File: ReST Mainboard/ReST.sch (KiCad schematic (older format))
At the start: 17 parts

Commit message: Added ReST connector to the Mainboard
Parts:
- added P?: CONN_02X04, symbol CONN_02X04
- added P? (x7): CONN_02X08, symbol CONN_02X08
- added P? (x4): CONN_02X10, symbol CONN_02X10
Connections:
- net labels added: +12V, +3.3V, +5V, E0-DIR, E0-EN, E0-MAX, E0-MIN, E0-STEP, E1-DIR, E1-EN, E1-MAX, E1-MIN, E1-STEP, E2-DIR, E2-EN, E2-MAX, E2-MIN, E2-STEP, E3-DIR, E3-EN, E3-MAX, E3-MIN, E3-STEP, PWM-BED, PWM-HEAT1, PWM-HEAT2, PWM-HEAT3, PWM-HEAT4, T0, T1, T2, T3, T4, X-DIR, X-EN, X-MAX, X-MIN, X-STEP, Y-DIR, Y-EN, Y-MAX, Y-MIN, Y-STEP, Z-DIR, Z-EN, Z-MAX, Z-MIN, Z-STEP
- wire segments 84 -> 302
- no-connect marks 0 -> 7
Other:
- note added: "Heatbed Connector"
- note added: "Heater Output 1"
- note added: "Heater Output 2"
- note added: "Heater Output 3"
- note added: "Heater Output 4"
- note added: "Stepper E0"
- note added: "Stepper E1"
- note added: "Stepper E2"
- note added: "Stepper E3"
- note added: "Stepper X"
- note added: "Stepper Y"
- note added: "Stepper Z"

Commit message: Added Pololu to the Mainboard
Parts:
- removed P? (x7): CONN_02X08, symbol CONN_02X08
- added C?: 10nF, symbol C_Small
- added C?: 100uF, symbol CP1_Small
- added P?: CONN_02X03, symbol CONN_02X03
- added P?: CONN_02X04, symbol CONN_02X04
- added P?: SCREW_01X04, symbol CONN_01X04
- added P?: CONN_01X03, symbol CONN_01X03
- added P? (x2): SCREW_01X03, symbol CONN_01X03
- added R?: 100K, symbol R_Small
- added U?: POLOLU_A4988, symbol POLOLU_A4988
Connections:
- net labels added: ENDSTOP_VCC
- net labels removed: E0-DIR, E0-EN, E0-MAX, E0-MIN, E0-STEP, E1-DIR, E1-EN, E1-MAX, E1-MIN, E1-STEP, E2-DIR, E2-EN, E2-MAX, E2-MIN, E2-STEP, E3-DIR, E3-EN, E3-MAX, E3-MIN, E3-STEP, X-DIR, X-EN, X-MAX, X-MIN, X-STEP, Y-DIR, Y-EN, Y-MAX, Y-MIN, Y-STEP, Z-DIR, Z-EN, Z-MAX, Z-MIN, Z-STEP
- wire segments 302 -> 227
- no-connect marks 7 -> 0
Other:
- note removed: "Stepper E0"
- note removed: "Stepper E1"
- note removed: "Stepper E2"
- note removed: "Stepper E3"
- note removed: "Stepper X"
- note removed: "Stepper Y"
- note removed: "Stepper Z"

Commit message: Changes to the mainboard
removed the pololu connector, added it onboard. added 5V regulator. need to add 3.3V Regulator and more pinout (Bluetooth, SWD, Boot0/Boot1 and more)
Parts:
- removed C? (x11): 100nF, symbol C_Small
- removed C?: 4.7uF, symbol C_Small
- removed C?: 10nF, symbol C_Small
- removed C?: 1uF, symbol C_Small
- removed I?: STM32F103ZET6, MODULE, symbol STM32F103ZET6
- removed L?: INDUCTOR_SMALL, symbol INDUCTOR_SMALL
- removed P? (x2): CONN_02X10, symbol CONN_02X10
- added C? (x4): 100uF, symbol CP1_Small
- added C? (x6): 10nF, symbol C_Small
- added C? (x6): 100nF, symbol C_Small
- added C?: 1uF, symbol C_Small
- added C?: 4.7uF, symbol C_Small
- added C?: 10uF, symbol C_Small
- added C?: 22uF, symbol C_Small
- added F?: F_Small, symbol F_Small
- added L?: INDUCTOR_SMALL, symbol INDUCTOR_SMALL
- added P? (x4): CONN_02X03, symbol CONN_02X03
- added P? (x4): CONN_02X04, symbol CONN_02X04
- added P? (x4): SCREW_01X04, symbol CONN_01X04
- added P? (x5): CONN_01X03, symbol CONN_01X03
- added P? (x5): SCREW_01X03, symbol CONN_01X03
- added P?: USB_OTG, symbol USB_OTG
- added P?: CONN_01X02, symbol CONN_01X02
- added R? (x5): 100K, symbol R_Small
- added R? (x2): 22R, symbol R_Small
- added U? (x4): POLOLU_A4988, symbol POLOLU_A4988
- added U?: STM32F103VE, LQFP100, symbol STM32F103VE
- added U?: USBLC6-2, symbol USBLC6-2
- added U?: AMS1117-5.0, symbol AP1117
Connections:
- net labels added: E0-DIR, E0-EN, E0-STEP, E1-DIR, E1-EN, E1-STEP, USBDM, USBDP, VREF, X-DIR, X-EN, X-MAX, X-MIN, X-STEP, Y-DIR, Y-EN, Y-MAX, Y-MIN, Y-STEP, Z-DIR, Z-EN, Z-MAX, Z-MIN, Z-STEP
- net labels removed: PWM-HEAT3, PWM-HEAT4, T3, T4
- wire segments 227 -> 345
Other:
- note added: "STEPPER"
- note removed: "Heater Output 3"
- note removed: "Heater Output 4"
- moved on the sheet: C?, P?, R?, U?, X?

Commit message: Added Buck & Power Pins
Buck Converter Added (Still need work on Diode, have to do the math later)
Power Distribution Pins added (4 Pins of  GND 12V 5V 3V3 each) for convenience (Leds and whatnot)
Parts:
- removed U?: AMS1117-5.0, symbol AP1117
- added C? (x2): 2.2uF, symbol C_Small
- added D?: Schottky TBD, symbol D_Schottky_Small
- added L?: 3.3uH, symbol INDUCTOR_SMALL
- added P? (x2): CONN_02X04, symbol CONN_02X04
- added R?: 100K, symbol R_Small
- added R? (x2): 20K, symbol R_Small
- added U?: LM7805, symbol LM7805
- added U?: LMR10515YMFX, SOT-23-5, symbol LMR10510YMF
- C?: value 10uF -> 1uF
- C?: value 22uF -> 100nF
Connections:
- wire segments 345 -> 382
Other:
- note added: "Power Distribution"
- moved on the sheet: C?, P?, R?, U?

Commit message: Added Addition Pinout
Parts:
- added P? (x7): CONN_01X03, symbol CONN_01X03
- added P?: CONN_02X06, symbol CONN_02X06
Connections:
- net +12V: now also P?.1 (P1), P?.3 (P3), P?.5 (P5), P?.7 (P7)
- net +3V3: now also P?.9 (P9)
- net +5V: now also P?.12 (P12), P?.2 (P2), P?.2 (P2), P?.2 (P2), P?.2 (P2), P?.2 (P2); no longer C?.2, U?.VO
- net GND: now also P?.11 (P11), P?.2 (P2), P?.3 (P3), P?.3 (P3), P?.3 (P3), P?.3 (P3), P?.4 (P4), P?.6 (P6), P?.8 (P8)
- net VCC: now reaches P?.1 (VCC)
- net VCC: now also P?.1 (P1)
- new net ADD: P?.10 (P10)
- new net BOOT0: P?.2 (P2)
- new net BOOT1: P?.2 (P2)
- new net SERVO1: P?.1 (P1)
- new net SERVO2: P?.1 (P1)
- new net SERVO3: P?.1 (P1)
- new net SERVO4: P?.1 (P1)
- new net VDD: C?.2, P?.3 (P3), U?.VO
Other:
- note added: "Additional Output"
- note added: "VCC: 5V over USB\nVDD: 5V over LDO (12V Rail)"

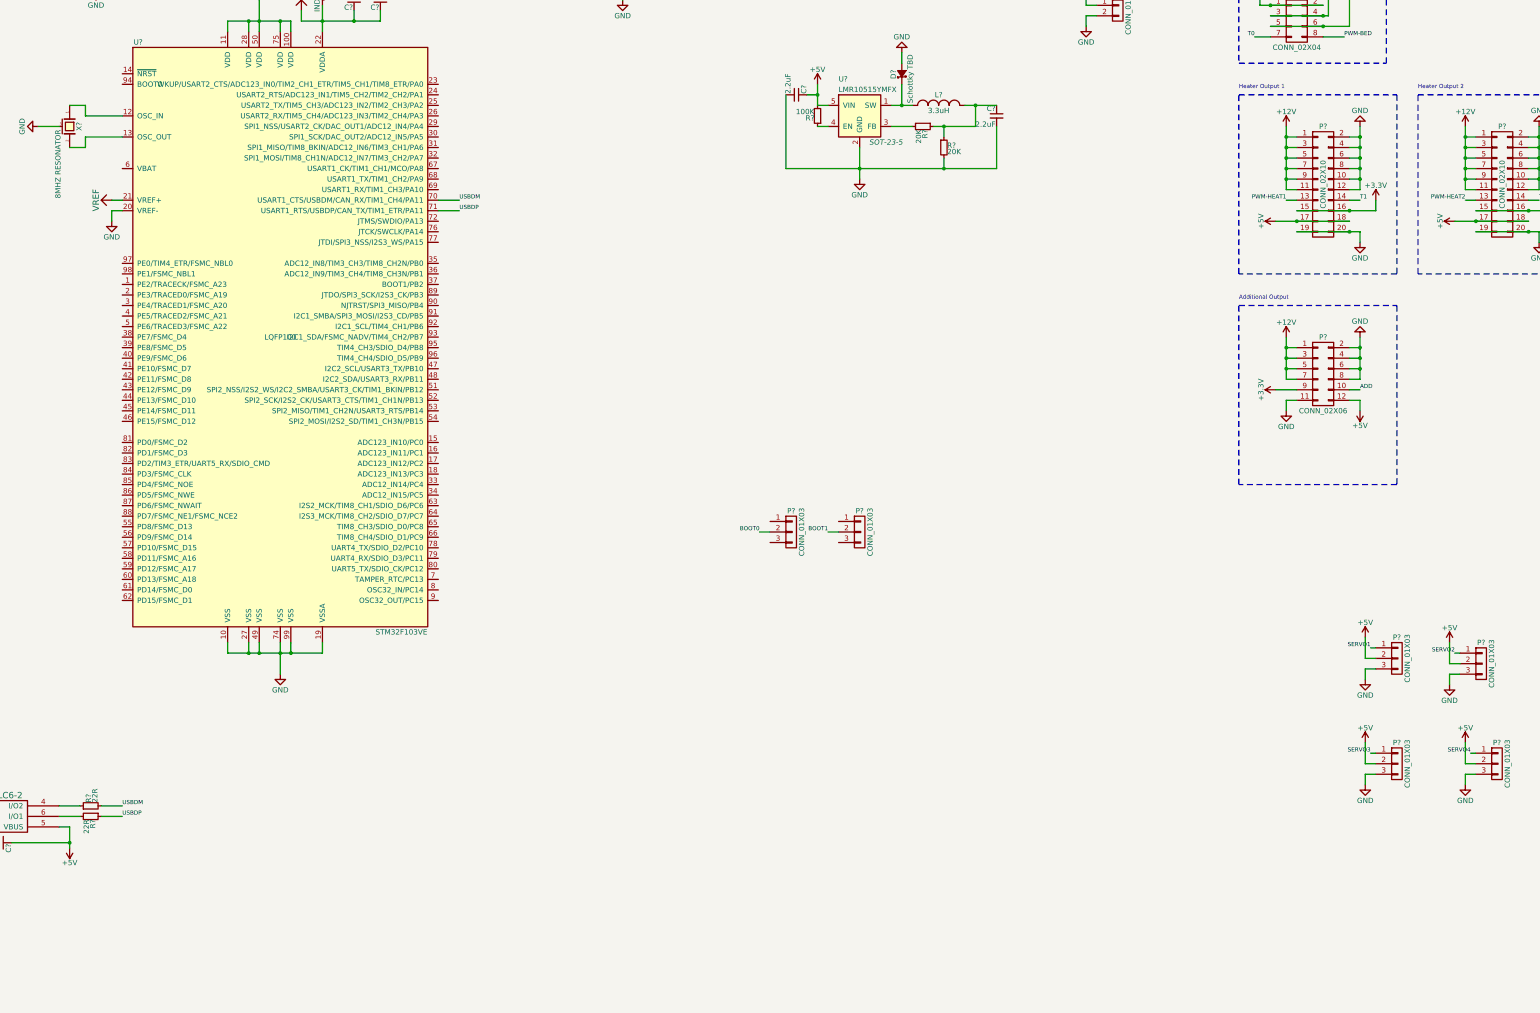
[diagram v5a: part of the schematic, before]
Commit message: Changed Additional-Board and Pinout
Sooo... I thought adding multiple Additional Module Boards would be bit much. Looked back at some older projects of mine and thought that using something like the uln2803 would be pretty neat (like 8 NPN Transitors, each 500mah and that in a DIL-18 Package IIRC) Which turns price really down, aswell as the size of the module. 
But using that one resultet in removing many extra pinouts, leaving with only 5 unused pins which will be broken out extra. This may change when the lcd pinout is finished. adding extra pinout for the additional board could also work out (as it occupies 8 pwm pins). I will look to copy that all into the schematic

Also missing: I2C EEPROM/Flash for settings
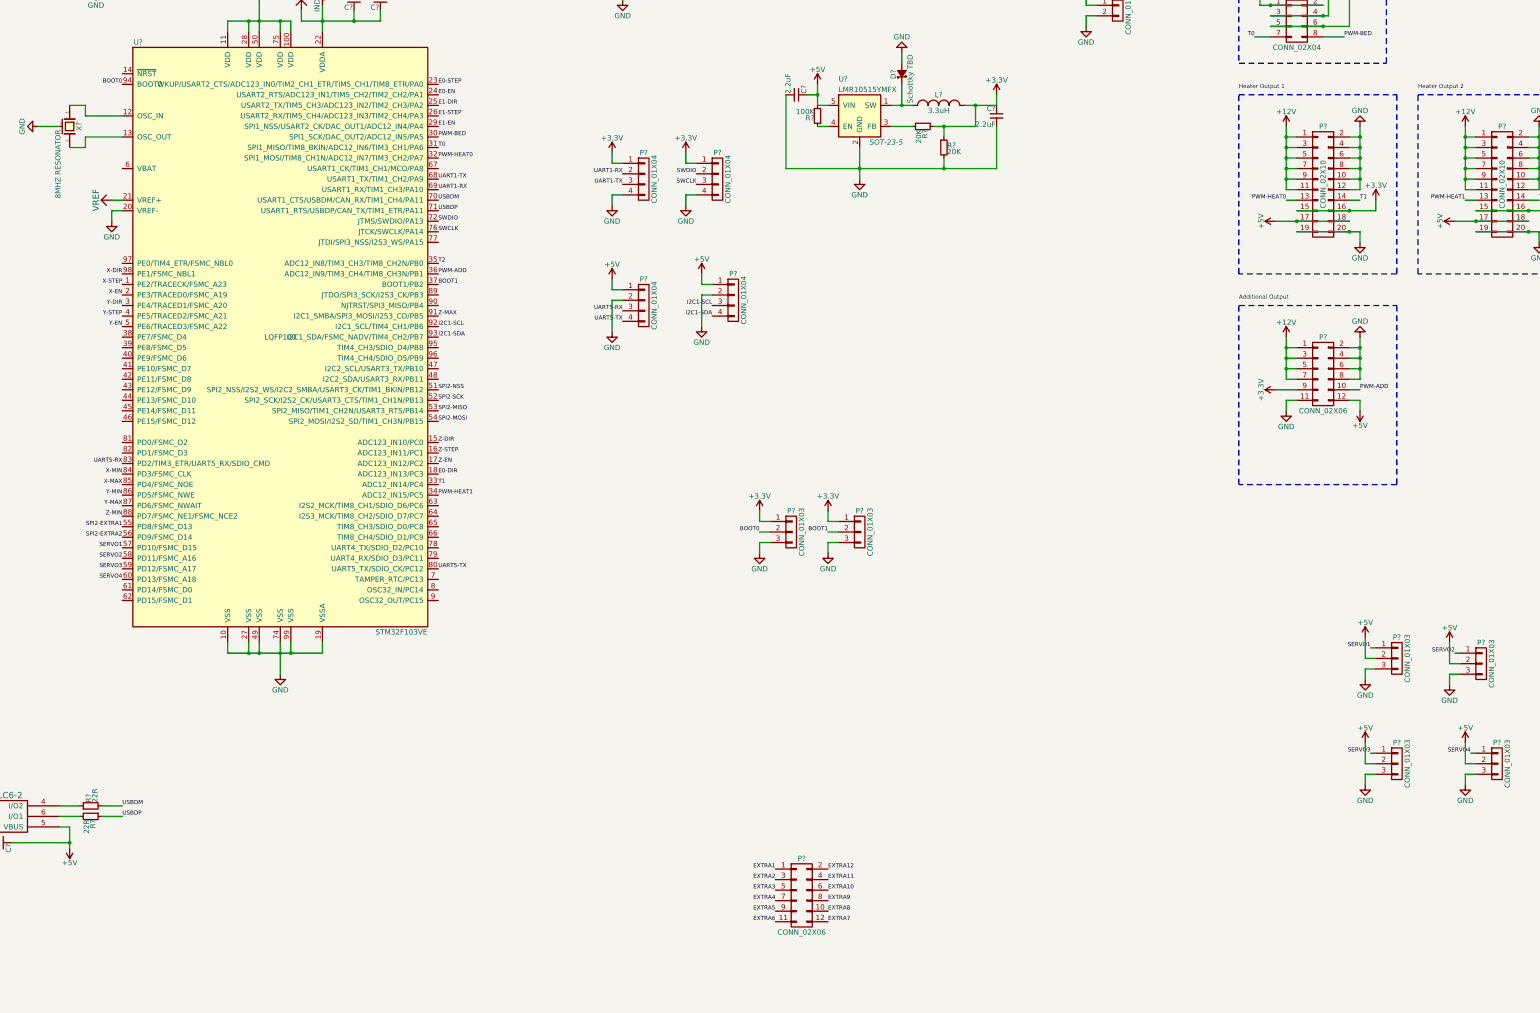
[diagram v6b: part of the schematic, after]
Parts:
- added P? (x4): CONN_01X04, symbol CONN_01X04
- added P?: CONN_02X06, symbol CONN_02X06
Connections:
- net ADD is gone; now on net PWM-ADD: P?.10 (P10)
- net PWM-HEAT2 is gone; now on net PWM-HEAT1: P?.13 (P13)
- net +3V3: now also C?.1, L?.2, P?.1 (P1), P?.1 (P1), R?.1, R?.1, P?.1 (P1), P?.1 (P1)
- net +5V: now also P?.1 (P1), P?.1 (P1)
- net BOOT0: now also U?.94 (BOOT0)
- net BOOT1: now also U?.37 (BOOT1/PB2)
- net E0-DIR: now also U?.18 (ADC123_IN13/PC3)
- net E0-EN: now also U?.24 (USART2_RTS/ADC123_IN1/TIM5_CH2/TIM2_CH2/PA1)
- net E0-STEP: now also U?.23 (WKUP/USART2_CTS/ADC123_IN0/TIM2_CH1_ETR/TIM5_CH1/TIM8_ETR/PA0)
- net E1-DIR: now also U?.25 (USART2_TX/TIM5_CH3/ADC123_IN2/TIM2_CH3/PA2)
- net E1-EN: now also U?.29 (SPI1_NSS/USART2_CK/DAC_OUT1/ADC12_IN4/PA4)
- net E1-STEP: now also U?.26 (USART2_RX/TIM5_CH4/ADC123_IN3/TIM2_CH4/PA3)
- net GND: now also P?.3 (P3), P?.3 (P3), P?.2 (P2), P?.2 (P2), P?.4 (P4), P?.4 (P4)
- net PWM-BED: now also U?.30 (SPI1_SCK/DAC_OUT2/ADC12_IN5/PA5)
- net PWM-HEAT1: now also U?.34 (ADC12_IN15/PC5); no longer P?.13 (P13)
- net SERVO1: now also U?.57 (PD10/FSMC_D15)
- net SERVO2: now also U?.58 (PD11/FSMC_A16)
- net SERVO3: now also U?.59 (PD12/FSMC_A17)
- net SERVO4: now also U?.60 (PD13/FSMC_A18)
- net T0: now also U?.31 (SPI1_MISO/TIM8_BKIN/ADC12_IN6/TIM3_CH1/PA6)
- net T1: now also U?.33 (ADC12_IN14/PC4)
- net T2: now also U?.35 (ADC12_IN8/TIM3_CH3/TIM8_CH2N/PB0)
- net X-DIR: now also U?.98 (PE1/FSMC_NBL1)
- net X-EN: now also U?.2 (PE3/TRACED0/FSMC_A19)
- net X-MAX: now also U?.85 (PD4/FSMC_NOE)
- net X-MIN: now also U?.84 (PD3/FSMC_CLK)
- net X-STEP: now also U?.1 (PE2/TRACECK/FSMC_A23)
- net Y-DIR: now also U?.3 (PE4/TRACED1/FSMC_A20)
- net Y-EN: now also U?.5 (PE6/TRACED3/FSMC_A22)
- net Y-MAX: now also U?.87 (PD6/FSMC_NWAIT)
- net Y-MIN: now also U?.86 (PD5/FSMC_NWE)
- net Y-STEP: now also U?.4 (PE5/TRACED2/FSMC_A21)
- net Z-DIR: now also U?.15 (ADC123_IN10/PC0)
- net Z-EN: now also U?.17 (ADC123_IN12/PC2)
- net Z-MAX: now also U?.91 (I2C1_SMBA/SPI3_MOSI/I2S3_CD/PB5)
- net Z-MIN: now also U?.88 (PD7/FSMC_NE1/FSMC_NCE2)
- net Z-STEP: now also U?.16 (ADC123_IN11/PC1)
- net PWM-HEAT0: now reaches U?.32 (SPI1_MOSI/TIM8_CH1N/ADC12_IN7/TIM3_CH2/PA7)
- net PWM-HEAT0: now also P?.13 (P13)
- net PWM-ADD: now reaches U?.36 (ADC12_IN9/TIM3_CH4/TIM8_CH3N/PB1)
- net SPI2-NSS: now reaches U?.51 (SPI2_NSS/I2S2_WS/I2C2_SMBA/USART3_CK/TIM1_BKIN/PB12)
- net SPI2-SCK: now reaches U?.52 (SPI2_SCK/I2S2_CK/USART3_CTS/TIM1_CH1N/PB13)
- net SPI2-MISO: now reaches U?.53 (SPI2_MISO/TIM1_CH2N/USART3_RTS/PB14)
- net SPI2-MOSI: now reaches U?.54 (SPI2_MOSI/I2S2_SD/TIM1_CH3N/PB15)
- net SPI2-EXTRA1: now reaches U?.55 (PD8/FSMC_D13)
- net SPI2-EXTRA2: now reaches U?.56 (PD9/FSMC_D14)
- net UART1-TX: now reaches U?.68 (USART1_TX/TIM1_CH2/PA9)
- net UART1-TX: now also P?.3 (P3)
- net UART1-RX: now reaches U?.69 (USART1_RX/TIM1_CH3/PA10)
- net UART1-RX: now also P?.2 (P2)
- net SWDIO: now reaches U?.72 (JTMS/SWDIO/PA13)
- net SWDIO: now also P?.2 (P2)
- net SWCLK: now reaches U?.76 (JTCK/SWCLK/PA14)
- net SWCLK: now also P?.3 (P3)
- net UART5-TX: now reaches U?.80 (UART5_TX/SDIO_CK/PC12)
- net UART5-TX: now also P?.4 (P4)
- net UART5-RX: now reaches U?.83 (PD2/TIM3_ETR/UART5_RX/SDIO_CMD)
- net UART5-RX: now also P?.3 (P3)
- net I2C1-SCL: now reaches U?.92 (I2C1_SCL/TIM4_CH1/PB6)
- net I2C1-SCL: now also P?.3 (P3)
- net I2C1-SDA: now reaches U?.93 (I2C1_SDA/FSMC_NADV/TIM4_CH2/PB7)
- net I2C1-SDA: now also P?.4 (P4)
- new net EXTRA1: P?.1 (P1)
- new net EXTRA10: P?.6 (P6)
- new net EXTRA11: P?.4 (P4)
- new net EXTRA12: P?.2 (P2)
- new net EXTRA2: P?.3 (P3)
- new net EXTRA3: P?.5 (P5)
- new net EXTRA4: P?.7 (P7)
- new net EXTRA5: P?.9 (P9)
- new net EXTRA6: P?.11 (P11)
- new net EXTRA7: P?.12 (P12)
- new net EXTRA8: P?.10 (P10)
- new net EXTRA9: P?.8 (P8)
